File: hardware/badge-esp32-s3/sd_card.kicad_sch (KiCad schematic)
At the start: 2 parts

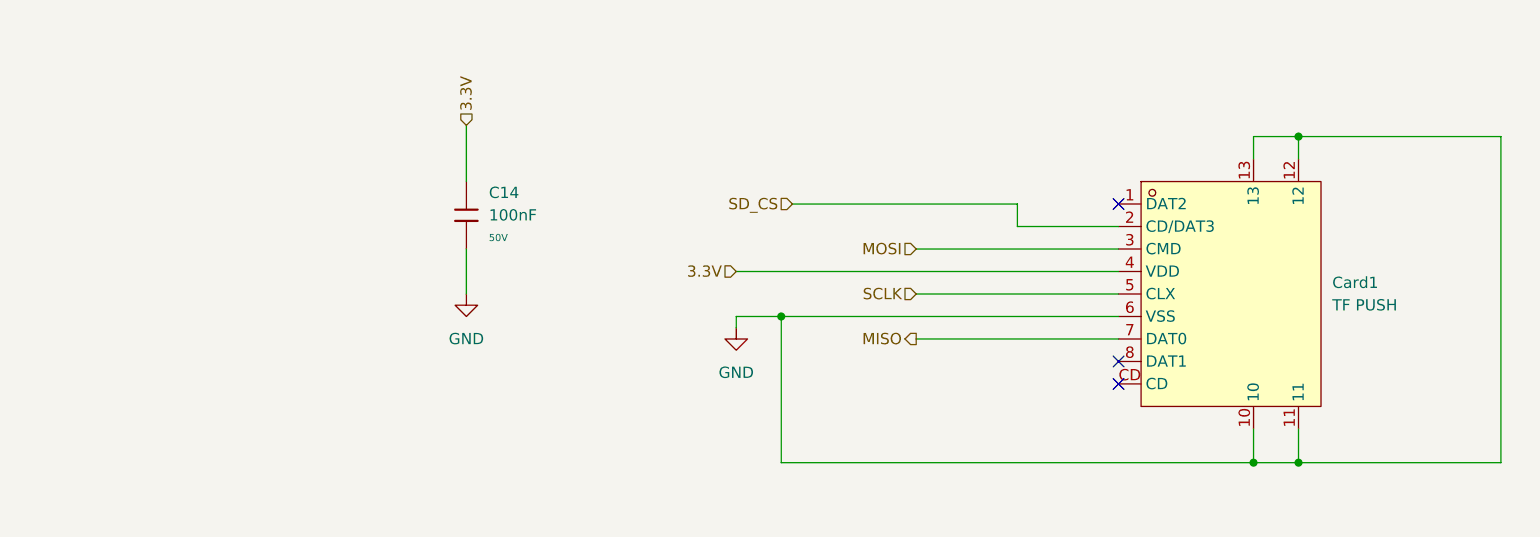
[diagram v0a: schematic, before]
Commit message: added sdio
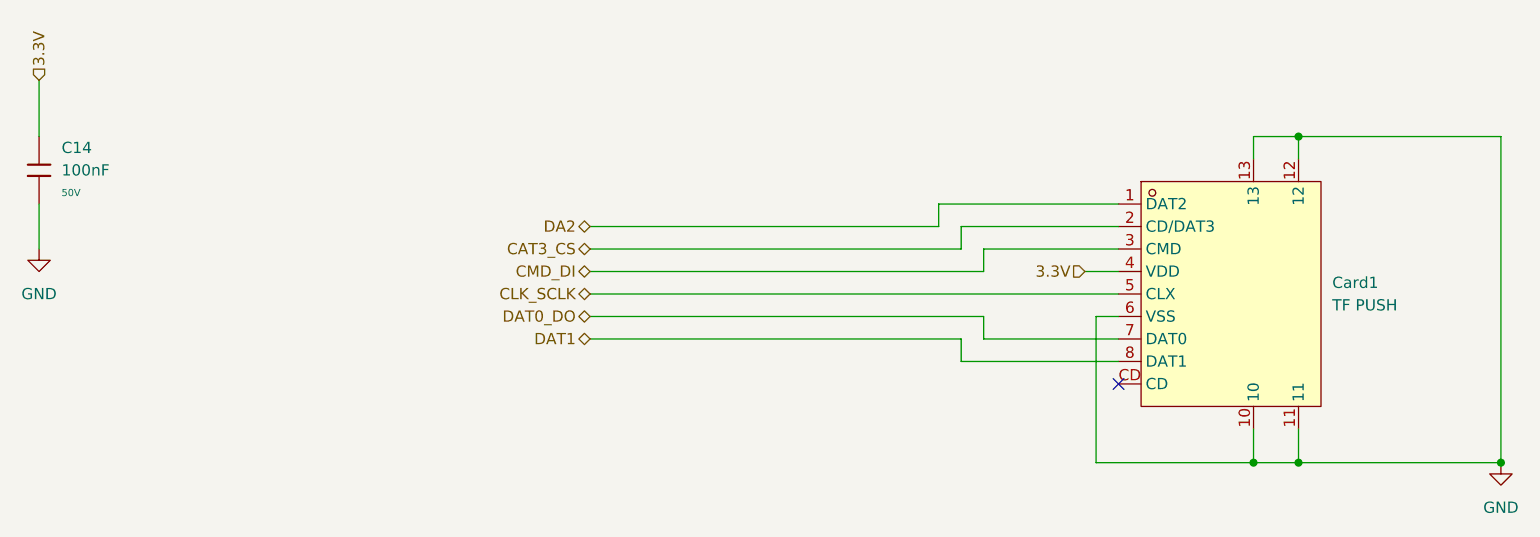
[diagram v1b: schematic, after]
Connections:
- net DA2: now reaches Card1.1 (DAT2)
- net DAT1: now reaches Card1.8 (DAT1)
- net MISO renamed DAT0_DO
- net MOSI renamed CMD_DI
- net SCLK renamed CLK_SCLK
- net SD_CS renamed CAT3_CS
- no-connect marks 3 -> 1
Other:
- moved on the sheet: C14

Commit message: almost finished
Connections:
- net 3.3V renamed 3.3v
- net CAT3_CS renamed SD_CS
- net CLK_SCLK renamed SCLK
- net CMD_DI renamed MOSI
- net DA2: no longer names the net of Card1.1 (DAT2)
- net DAT0_DO renamed MISO
- net DAT1: no longer names the net of Card1.8 (DAT1)
- no-connect marks 1 -> 3
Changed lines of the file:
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@@
 	(paper "A4")
-	(junction
-		(at 187.96 76.2)
-		(diameter 0)
-		(color 0 0 0 0)
-	)
 	(junction
 		(at 193.04 39.37)
@@
 		(at 172.72 67.31)
 	)
-	(wire
-		(pts
-			(xy 168.91 54.61) (xy 172.72 54.61)
-		)
-		(stroke
-			(width 0)
-			(type default)
-		)
-	)
-	(wire
-		(pts
-			(xy 172.72 62.23) (xy 157.48 62.23)
+	(no_connect
+		(at 172.72 46.99)
+	)
+	(no_connect
+		(at 172.72 64.77)
+	)
+	(wire
+		(pts
+			(xy 160.02 59.69) (xy 160.02 68.58)
 		)
 		(stroke
@@
 	(wire
 		(pts
+			(xy 133.35 62.23) (xy 172.72 62.23)
+		)
+		(stroke
+			(width 0)
+			(type default)
+		)
+	)
+	(wire
+		(pts
 			(xy 193.04 39.37) (xy 193.04 41.91)
 		)
@@
 	(wire
 		(pts
-			(xy 113.03 57.15) (xy 172.72 57.15)
-		)
-		(stroke
-			(width 0)
-			(type default)
-		)
-	)
-	(wire
-		(pts
-			(xy 172.72 64.77) (xy 154.94 64.77)
-		)
-		(stroke
-			(width 0)
-			(type default)
-		)
-	)
-	(wire
-		(pts
-			(xy 172.72 49.53) (xy 154.94 49.53)
-		)
-		(stroke
-			(width 0)
-			(type default)
-		)
-	)
-	(wire
-		(pts
-			(xy 170.18 76.2) (xy 187.96 76.2)
-		)
-		(stroke
-			(width 0)
-			(type default)
-		)
-	)
-	(wire
-		(pts
-			(xy 154.94 62.23) (xy 113.03 62.23)
-		)
-		(stroke
-			(width 0)
-			(type default)
-		)
-	)
-	(wire
-		(pts
-			(xy 157.48 52.07) (xy 157.48 54.61)
-		)
-		(stroke
-			(width 0)
-			(type default)
-		)
-	)
-	(wire
-		(pts
-			(xy 152.4 46.99) (xy 152.4 49.53)
-		)
-		(stroke
-			(width 0)
-			(type default)
-		)
-	)
-	(wire
-		(pts
-			(xy 154.94 64.77) (xy 154.94 62.23)
-		)
-		(stroke
-			(width 0)
-			(type default)
-		)
-	)
-	(wire
-		(pts
-			(xy 172.72 52.07) (xy 157.48 52.07)
+			(xy 133.35 52.07) (xy 172.72 52.07)
+		)
+		(stroke
+			(width 0)
+			(type default)
+		)
+	)
+	(wire
+		(pts
+			(xy 172.72 59.69) (xy 160.02 59.69)
 		)
 		(stroke
@@
 	(wire
 		(pts
-			(xy 152.4 49.53) (xy 113.03 49.53)
-		)
-		(stroke
-			(width 0)
-			(type default)
-		)
-	)
-	(wire
-		(pts
-			(xy 157.48 62.23) (xy 157.48 59.69)
-		)
-		(stroke
-			(width 0)
-			(type default)
-		)
-	)
-	(wire
-		(pts
 			(xy 215.9 39.37) (xy 193.04 39.37)
 		)
@@
 	(wire
 		(pts
-			(xy 157.48 59.69) (xy 113.03 59.69)
+			(xy 133.35 57.15) (xy 172.72 57.15)
 		)
 		(stroke
@@
 	(wire
 		(pts
+			(xy 133.35 49.53) (xy 172.72 49.53)
+		)
+		(stroke
+			(width 0)
+			(type default)
+		)
+	)
+	(wire
+		(pts
 			(xy 50.8 46.99) (xy 50.8 52.07)
 		)
@@
 	(wire
 		(pts
-			(xy 154.94 52.07) (xy 113.03 52.07)
-		)
-		(stroke
-			(width 0)
-			(type default)
-		)
-	)
-	(wire
-		(pts
 			(xy 193.04 72.39) (xy 193.04 76.2)
 		)
@@
 	(wire
 		(pts
-			(xy 157.48 54.61) (xy 113.03 54.61)
-		)
-		(stroke
-			(width 0)
-			(type default)
-		)
-	)
-	(wire
-		(pts
-			(xy 172.72 46.99) (xy 152.4 46.99)
-		)
-		(stroke
-			(width 0)
-			(type default)
-		)
-	)
-	(wire
-		(pts
-			(xy 154.94 49.53) (xy 154.94 52.07)
-		)
-		(stroke
-			(width 0)
-			(type default)
-		)
-	)
-	(wire
-		(pts
 			(xy 215.9 76.2) (xy 193.04 76.2)
 		)
@@
 	(wire
 		(pts
-			(xy 170.18 59.69) (xy 170.18 76.2)
-		)
-		(stroke
-			(width 0)
-			(type default)
-		)
-	)
-	(wire
-		(pts
-			(xy 172.72 59.69) (xy 170.18 59.69)
-		)
-		(stroke
-			(width 0)
-			(type default)
-		)
-	)
-	(hierarchical_label "DA2"
-		(shape bidirectional)
-		(at 113.03 49.53 180)
+			(xy 160.02 54.61) (xy 172.72 54.61)
+		)
+		(stroke
+			(width 0)
+			(type default)
+		)
+	)
+	(wire
+		(pts
+			(xy 160.02 44.45) (xy 160.02 54.61)
+		)
+		(stroke
+			(width 0)
+			(type default)
+		)
+	)
+	(hierarchical_label "MOSI"
+		(shape input)
+		(at 133.35 52.07 180)
 		(effects
 			(font
@@
 		)
 	)
-	(hierarchical_label "CMD_DI"
-		(shape bidirectional)
-		(at 113.03 54.61 180)
-		(effects
-			(font
-				(size 1.27 1.27)
-			)
-			(justify right)
-		)
-	)
-	(hierarchical_label "DAT0_DO"
-		(shape bidirectional)
-		(at 113.03 59.69 180)
-		(effects
-			(font
-				(size 1.27 1.27)
-			)
-			(justify right)
-		)
-	)
-	(hierarchical_label "DAT1"
-		(shape bidirectional)
-		(at 113.03 62.23 180)
-		(effects
-			(font
-				(size 1.27 1.27)
-			)
-			(justify right)
-		)
-	)
-	(hierarchical_label "3.3V"
+	(hierarchical_label "3.3v"
 		(shape input)
 		(at 50.8 33.02 90)
@@
 		)
 	)
-	(hierarchical_label "CAT3_CS"
-		(shape bidirectional)
-		(at 113.03 52.07 180)
+	(hierarchical_label "SCLK"
+		(shape input)
+		(at 133.35 57.15 180)
 		(effects
 			(font
@@
 		)
 	)
-	(hierarchical_label "CLK_SCLK"
-		(shape bidirectional)
-		(at 113.03 57.15 180)
+	(hierarchical_label "MISO"
+		(shape input)
+		(at 133.35 62.23 180)
 		(effects
 			(font
@@
 		)
 	)
-	(hierarchical_label "3.3V"
+	(hierarchical_label "SD_CS"
 		(shape input)
-		(at 168.91 54.61 180)
+		(at 133.35 49.53 180)
 		(effects
 			(font
@@
 			)
 			(justify right)
+		)
+	)
+	(hierarchical_label "3.3v"
+		(shape input)
+		(at 160.02 44.45 90)
+		(effects
+			(font
+				(size 1.27 1.27)
+			)
+			(justify left)
 		)
 	)
@@
 					(unit 1)
 				)
+			)
+		)
+	)
+	(symbol
+		(lib_id "power:GND")
+		(at 160.02 68.58 0)
+		(unit 1)
+		(exclude_from_sim no)
+		(in_bom yes)
+		(on_board yes)
+		(dnp no)
+		(property "Reference" "#PWR049"
+			(at 160.02 74.93 0)
+			(effects
+				(font
+					(size 1.27 1.27)
+				)
+				(hide yes)
+			)
+		)
+		(property "Value" "GND"
+			(at 160.02 72.39 0)
+			(effects
+				(font
+					(size 1.27 1.27)
+				)
+			)
+		)
+		(property "Footprint" ""
+			(at 160.02 68.58 0)
+			(effects
+				(font
+					(size 1.27 1.27)
+				)
+				(hide yes)
+			)
+		)
+		(property "Datasheet" ""
+			(at 160.02 68.58 0)
+			(effects
+				(font
+					(size 1.27 1.27)
+				)
+				(hide yes)
+			)
+		)
+		(property "Description" "Power symbol creates a global label with name \"GND\" , ground"
+			(at 160.02 68.58 0)
+			(effects
+				(font
+					(size 1.27 1.27)
+				)
+				(hide yes)
+			)
+		)
+		(pin "1"
+		)
+		(instances
+			(project ""
+				(path "/e2af9a6c-dbe9-4de2-9ba6-ea213a7300ec/61971e93-08b4-4717-9ec8-ac07d8e404d2"
+					(reference "#PWR049")
+					(unit 1)
+				)
